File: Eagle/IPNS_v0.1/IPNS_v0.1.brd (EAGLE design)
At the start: 32.7 x 33 mm, 30 parts, among them J1 SWIM, J2 NFC, J3 BATT, J4 LEFT CONN, J5 RIGHT CONN, Q1 16MHz, Q2 32.768 kHz, U1 STM8L152C4_C6TX

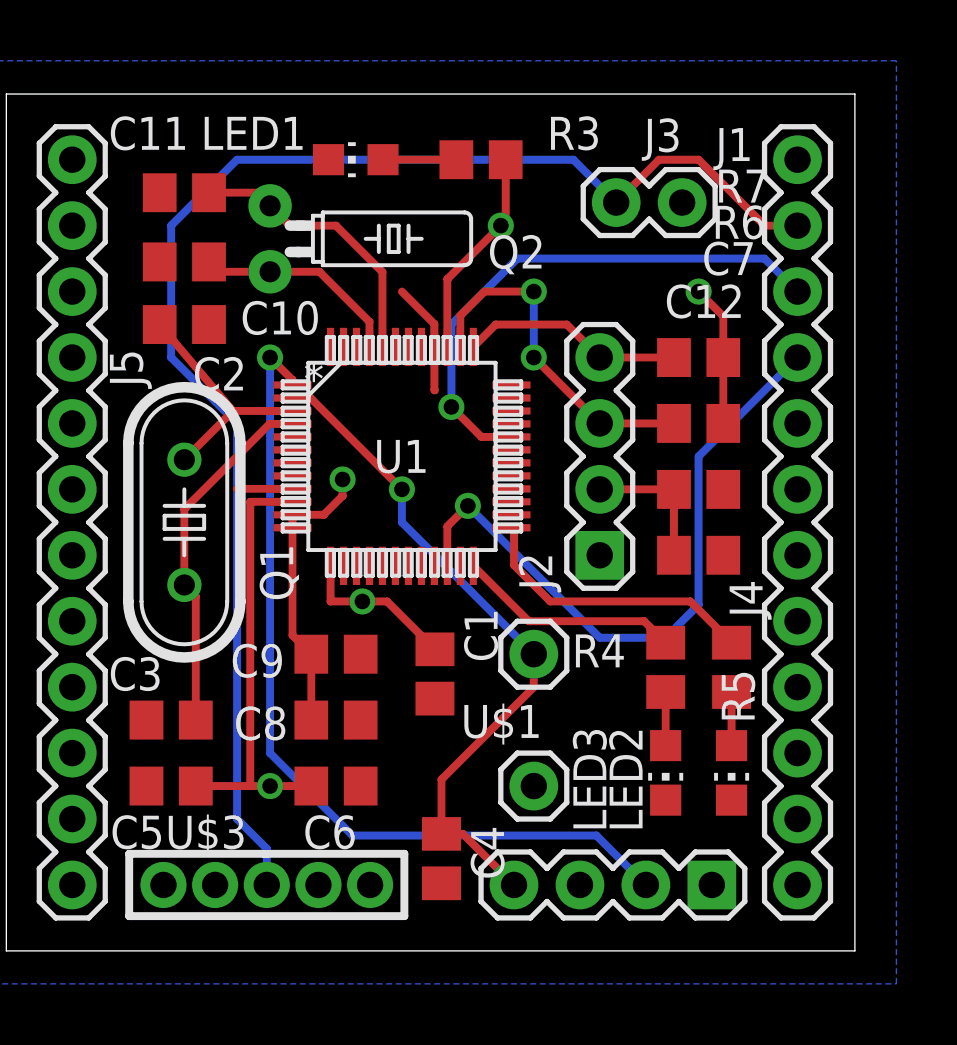
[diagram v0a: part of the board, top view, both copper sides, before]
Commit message: Board and schematic overall finished for MCU module. Need to check RC values
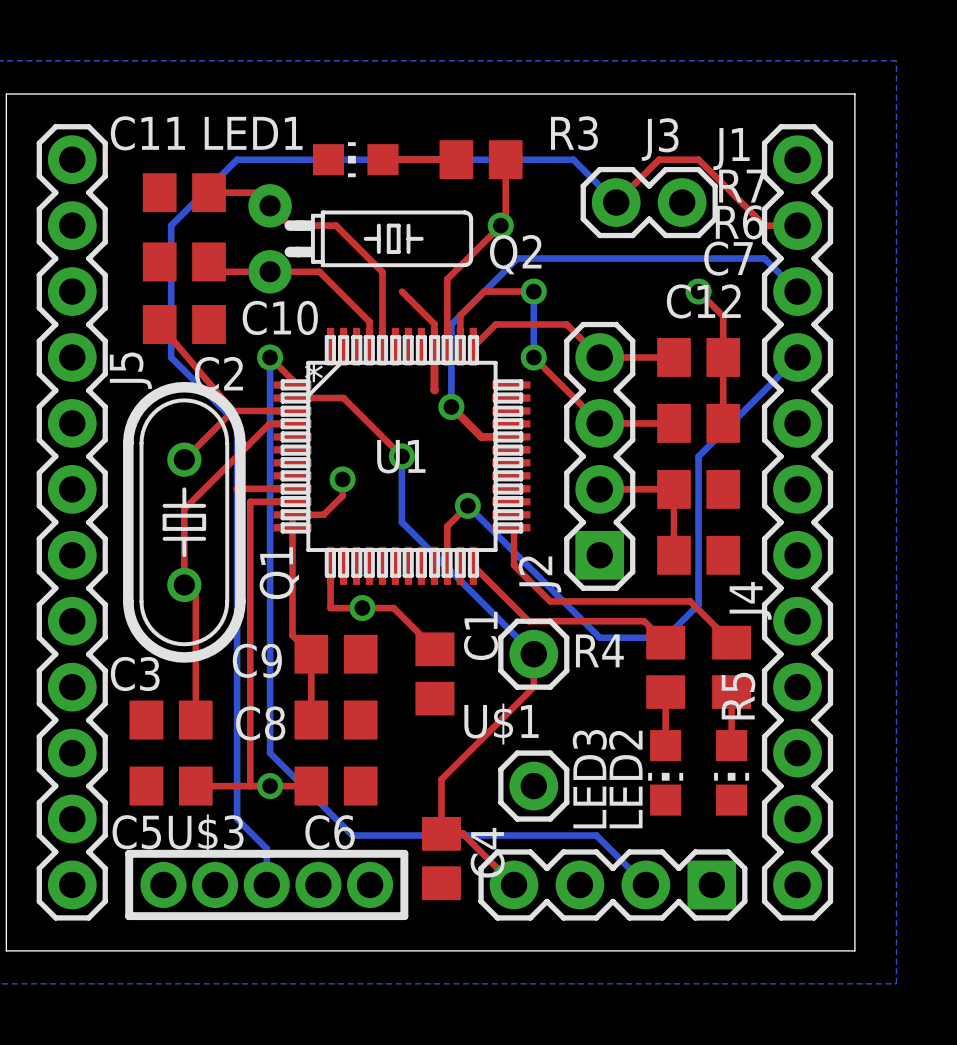
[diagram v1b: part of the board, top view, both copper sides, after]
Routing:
- net RESET: track 26.5 -> 27.9 mm
